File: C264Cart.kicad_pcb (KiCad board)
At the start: 2 copper layers, 55.8 x 91.4 mm, 13 parts, among them U1 27C040, U3 264-Exp-Port

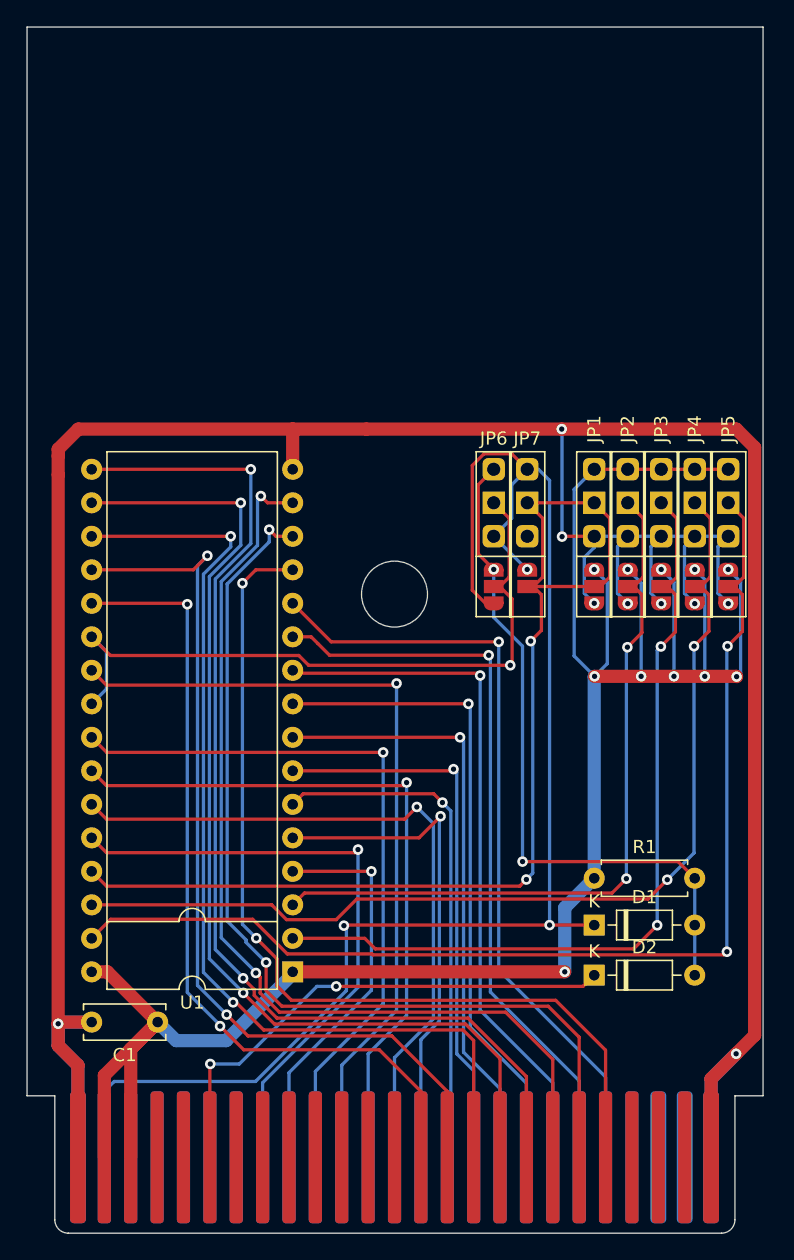
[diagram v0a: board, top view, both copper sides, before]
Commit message: Working to use a single 'modern' 27C512-27C040 EEPROM.
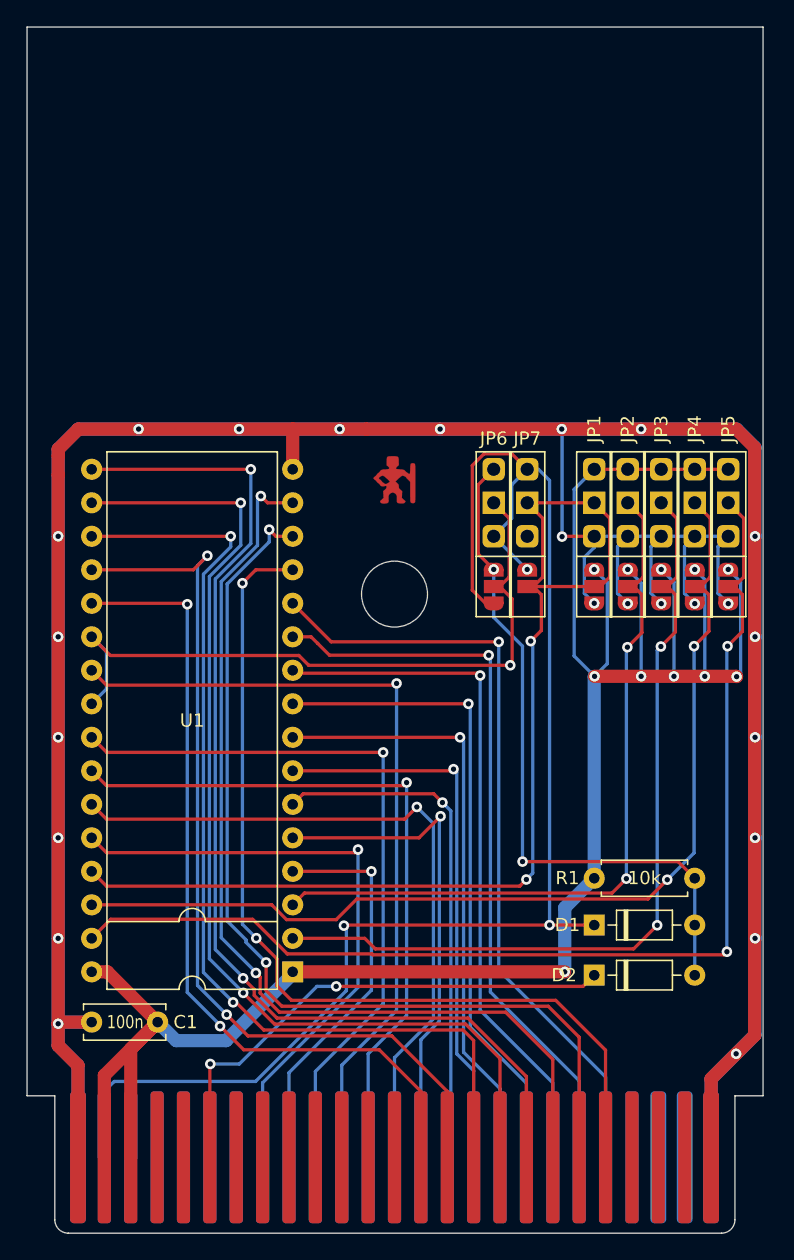
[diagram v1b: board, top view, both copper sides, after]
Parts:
- added G***: LOGO, Logo:bigby2-cu, F.Cu at (130.0, 78.6)
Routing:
- net GND: track 240.6 -> 384.8 mm, vias 9 -> 24

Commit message: Working to use a single 'modern' 27C512-27C040 EEPROM.
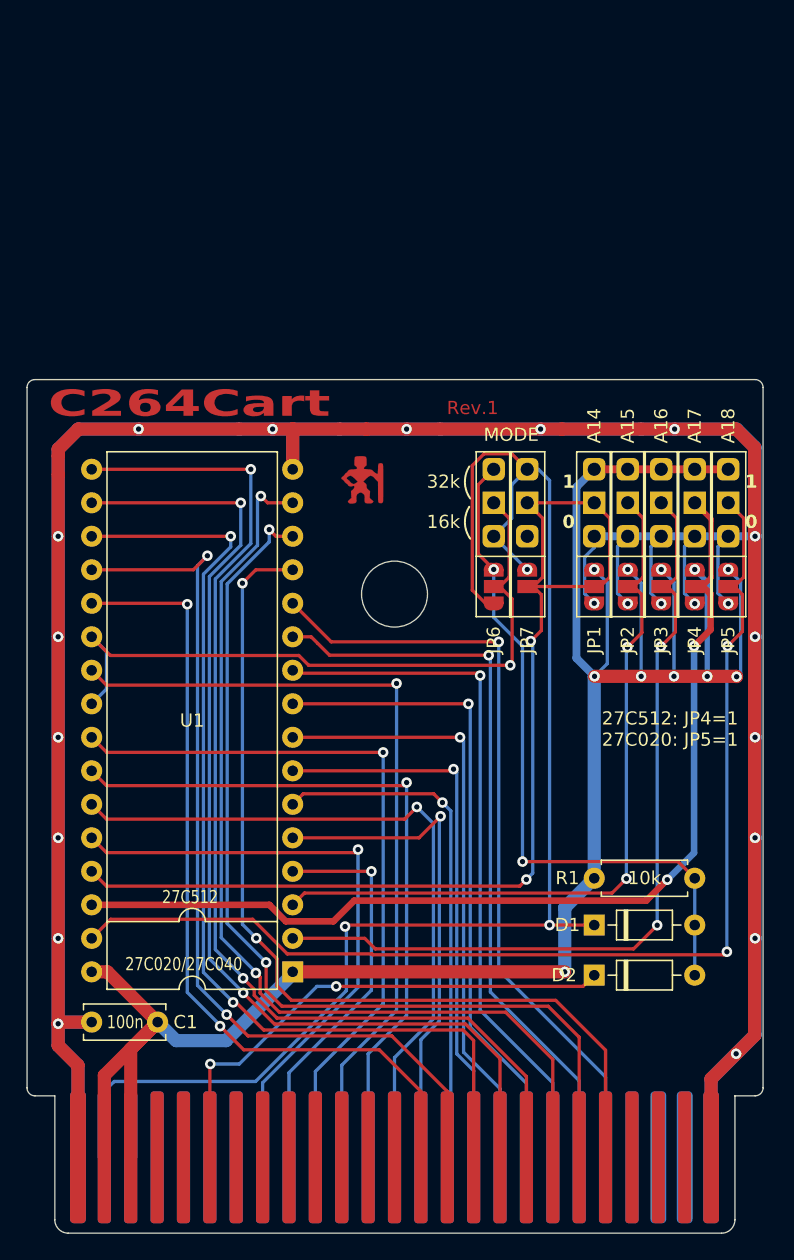
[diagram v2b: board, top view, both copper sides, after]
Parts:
- moved G*** 2.44 mm to (127.5, 78.6)
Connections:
- net Net-(JP1-C) renamed /A14
- net Net-(JP2-C) renamed /A15
- net Net-(JP3-C) renamed /A16
- net Net-(JP4-C) renamed /A17
- net Net-(JP5-C) renamed /A18
- net Net-(JP6-C) renamed /CE
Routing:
- net GND: track 384.8 -> 379.3 mm, vias 24 -> 22
- net /A17: track 76.7 -> 77.6 mm
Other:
- board size 55.8 x 91.4 mm -> 55.8 x 64.7 mm
- board text added: "0"
- board text added: "1"
- board text added: "16k"
- board text added: "27C020/27C040"
- board text added: "27C512"
- board text added: "27C512: JP4=1 27C020: JP5=1"
- board text added: "32k"
- board text added: "C264Cart"
- board text added: "MODE"
- board text added: "Rev.1"
- board text added: "github.com/hackup/C264Cart"

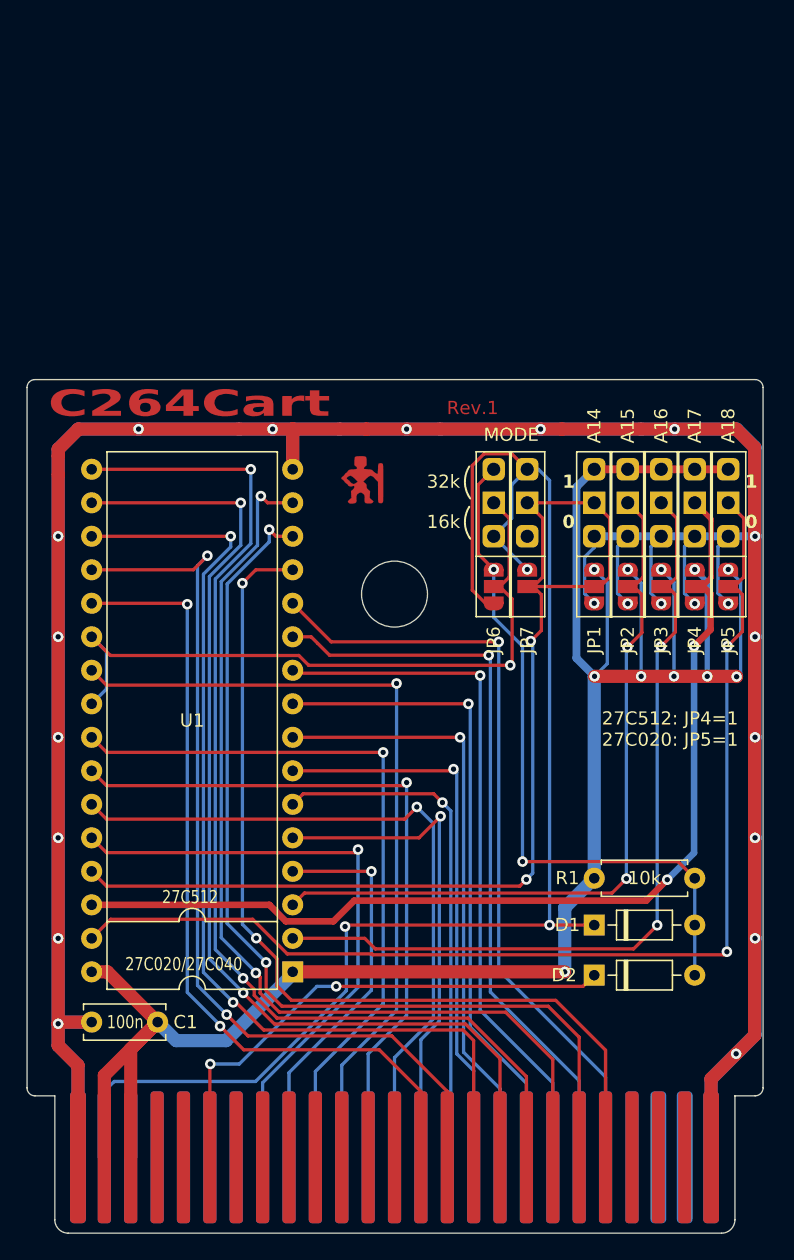
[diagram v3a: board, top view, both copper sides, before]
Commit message: Working to use a single 'modern' 27C512-27C040 EEPROM.
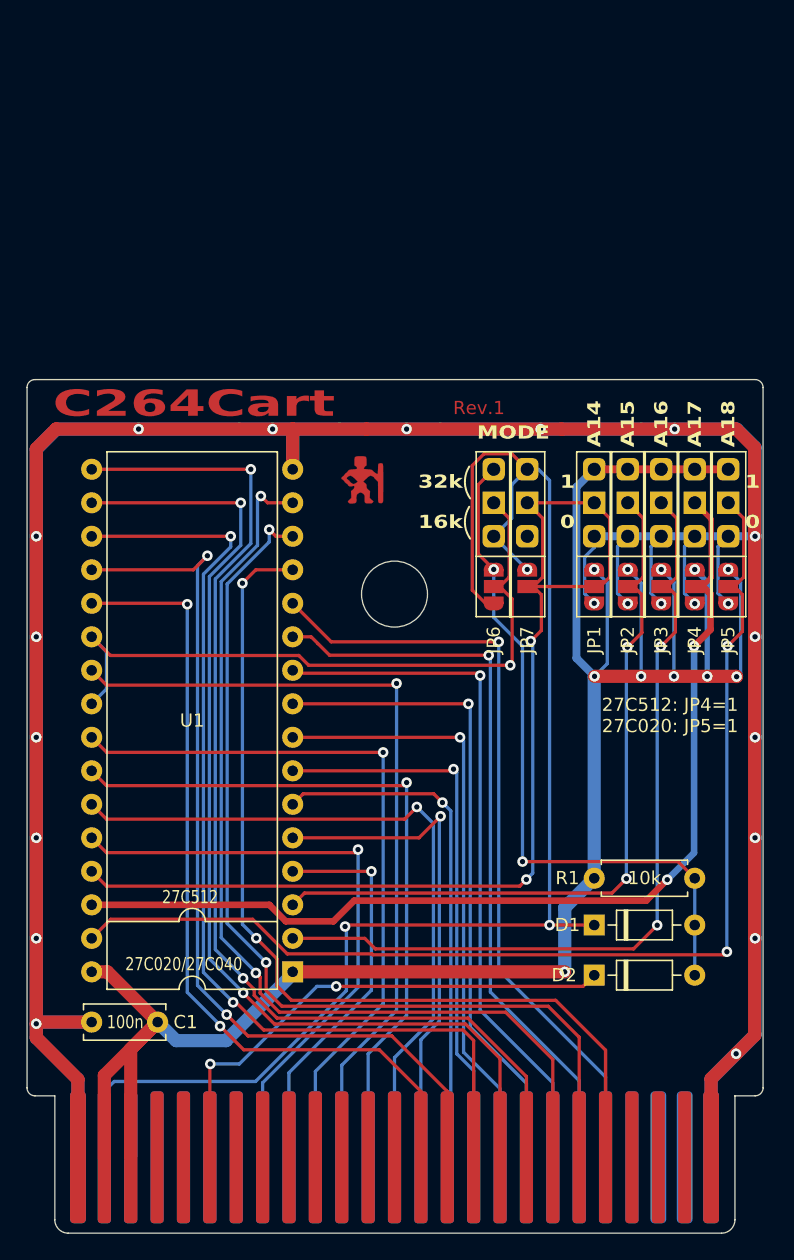
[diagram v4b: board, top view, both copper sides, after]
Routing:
- net GND: track 379.3 -> 387.3 mm
